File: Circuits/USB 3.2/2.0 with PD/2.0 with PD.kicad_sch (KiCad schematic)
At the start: 4 parts, among them P1 USB_C_Plug

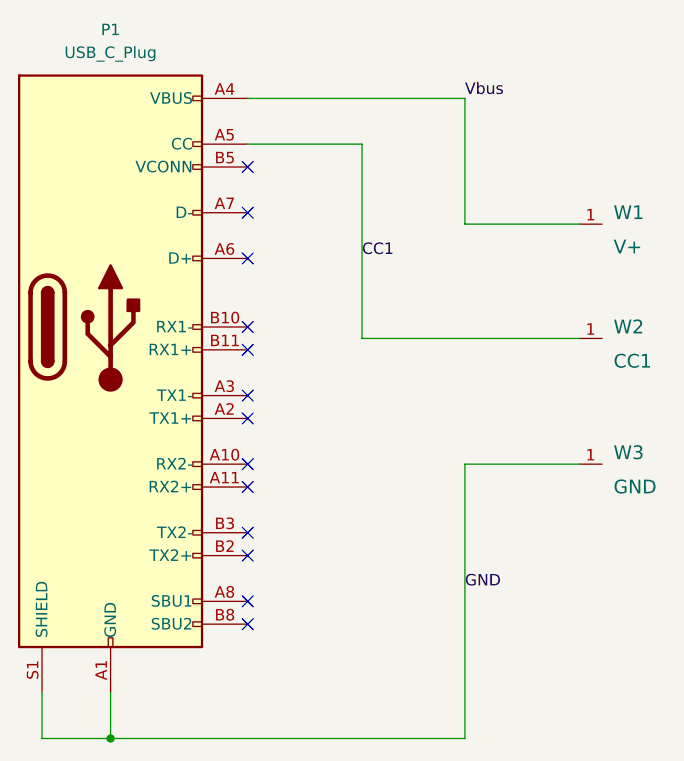
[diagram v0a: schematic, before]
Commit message: Working on USB 3.2
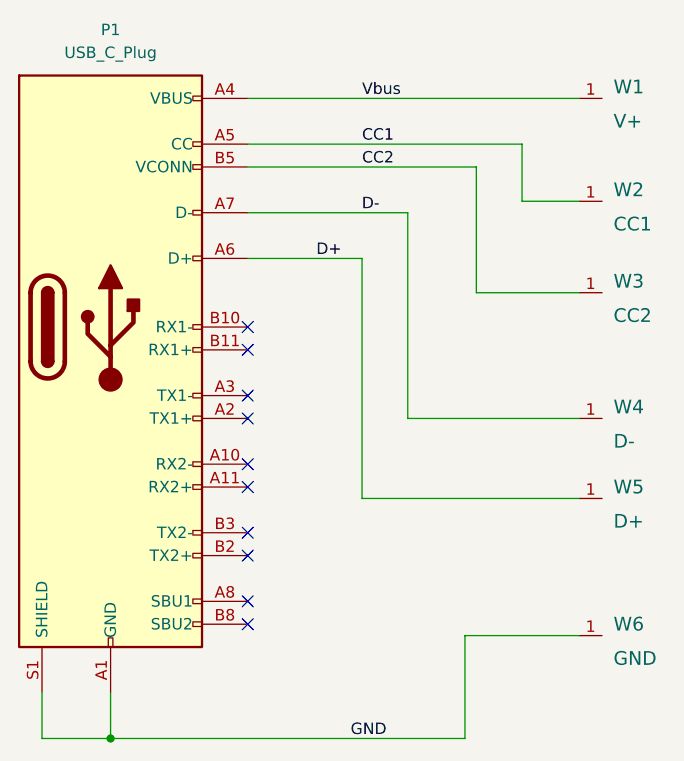
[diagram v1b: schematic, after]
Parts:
- added W3: CC2, Footprints:Pad_Small, symbol Ehryk:WIRE
- added W4: D-, Footprints:Pad_Small, symbol Ehryk:WIRE
- added W5: D+, Footprints:Pad_Small, symbol Ehryk:WIRE
- renumbered W3 to W6
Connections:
- net D+: now reaches P1.A6 (D+)
- net D+: now also W5.1
- net D-: now reaches P1.A7 (D-)
- net D-: now also W4.1
- net CC2: now reaches P1.B5 (VCONN)
- net CC2: now also W3.1
- no-connect marks 13 -> 10
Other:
- moved on the sheet: W1, W2, W6
